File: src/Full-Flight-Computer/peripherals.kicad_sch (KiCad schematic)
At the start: 36 parts, among them P10 Micro_SD_Card, P8 USB, P9 1984659, Q5 QS5U17TR, Q6 QS5U17TR, U10 TS391IYLT, U11 TS391IYLT, U6 SST25VF040B-50-4I-S2AE-T, U7 RFM95W-868S2, U8 CP2102-GMR(QFN28), U9 TS391IYLT

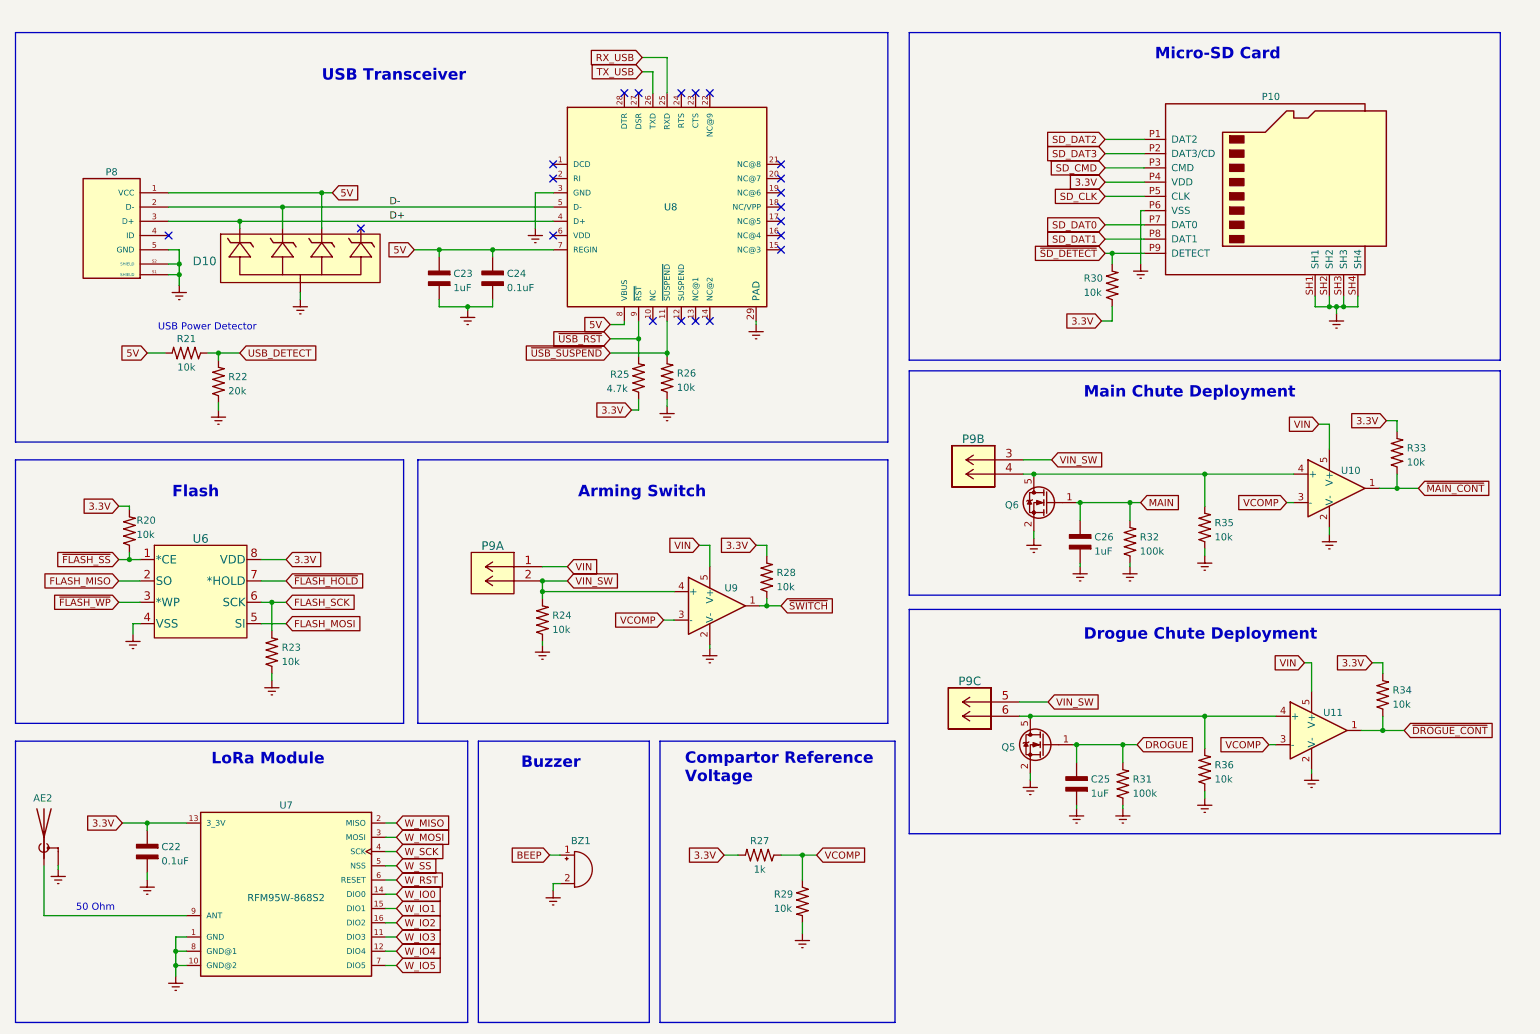
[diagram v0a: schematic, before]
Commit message: removed extra sections from schematic
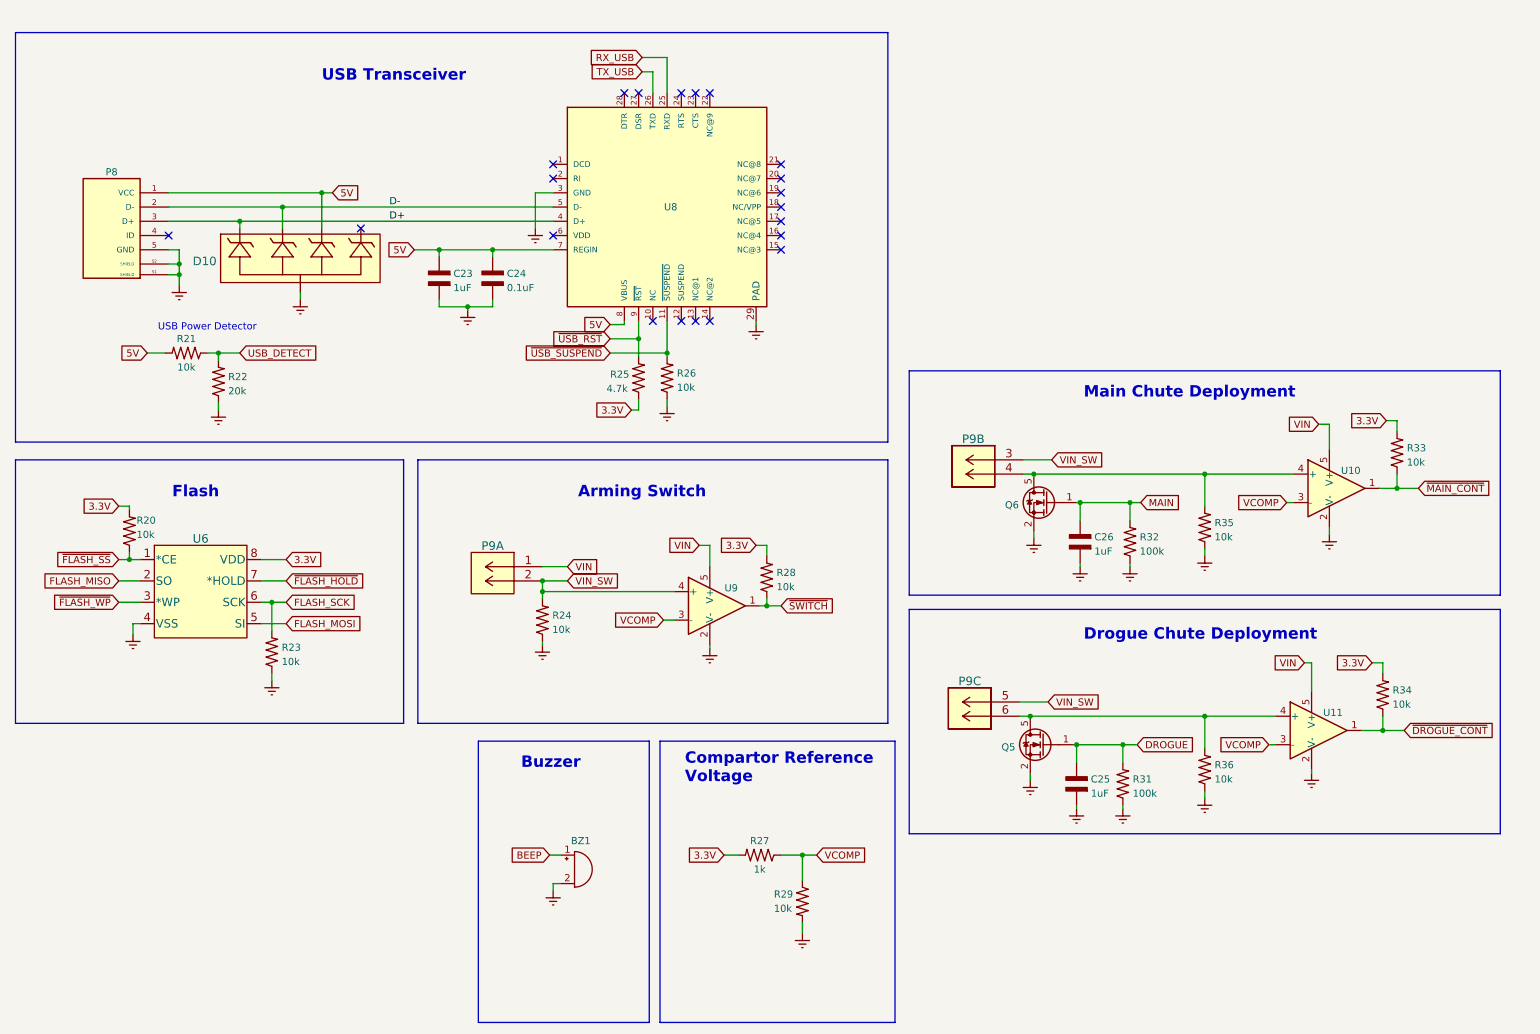
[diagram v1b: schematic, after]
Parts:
- removed AE2: 142-0701-851, Flight-Computer:142-0701-851, symbol Flight-Computer:142-0701-851
- removed C22: 0.1uF, Flight-Computer:CAP_0603, symbol Flight-Computer:CAP_0603
- removed P10: Micro_SD_Card, Flight-Computer:MEM2075-00-140-01-A, symbol Flight-Computer:Micro_SD_Card
- removed R30: 10k, Flight-Computer:RES_0603, symbol Flight-Computer:RES_0603
- removed U7: RFM95W-868S2, Flight-Computer:RFM95, symbol Flight-Computer:RFM95W-868S2
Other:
- note removed: "50 Ohm"
- note removed: "LoRa Module"
- note removed: "Micro-SD Card"

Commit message: fixed all schematic symbol links to link to correct lib file
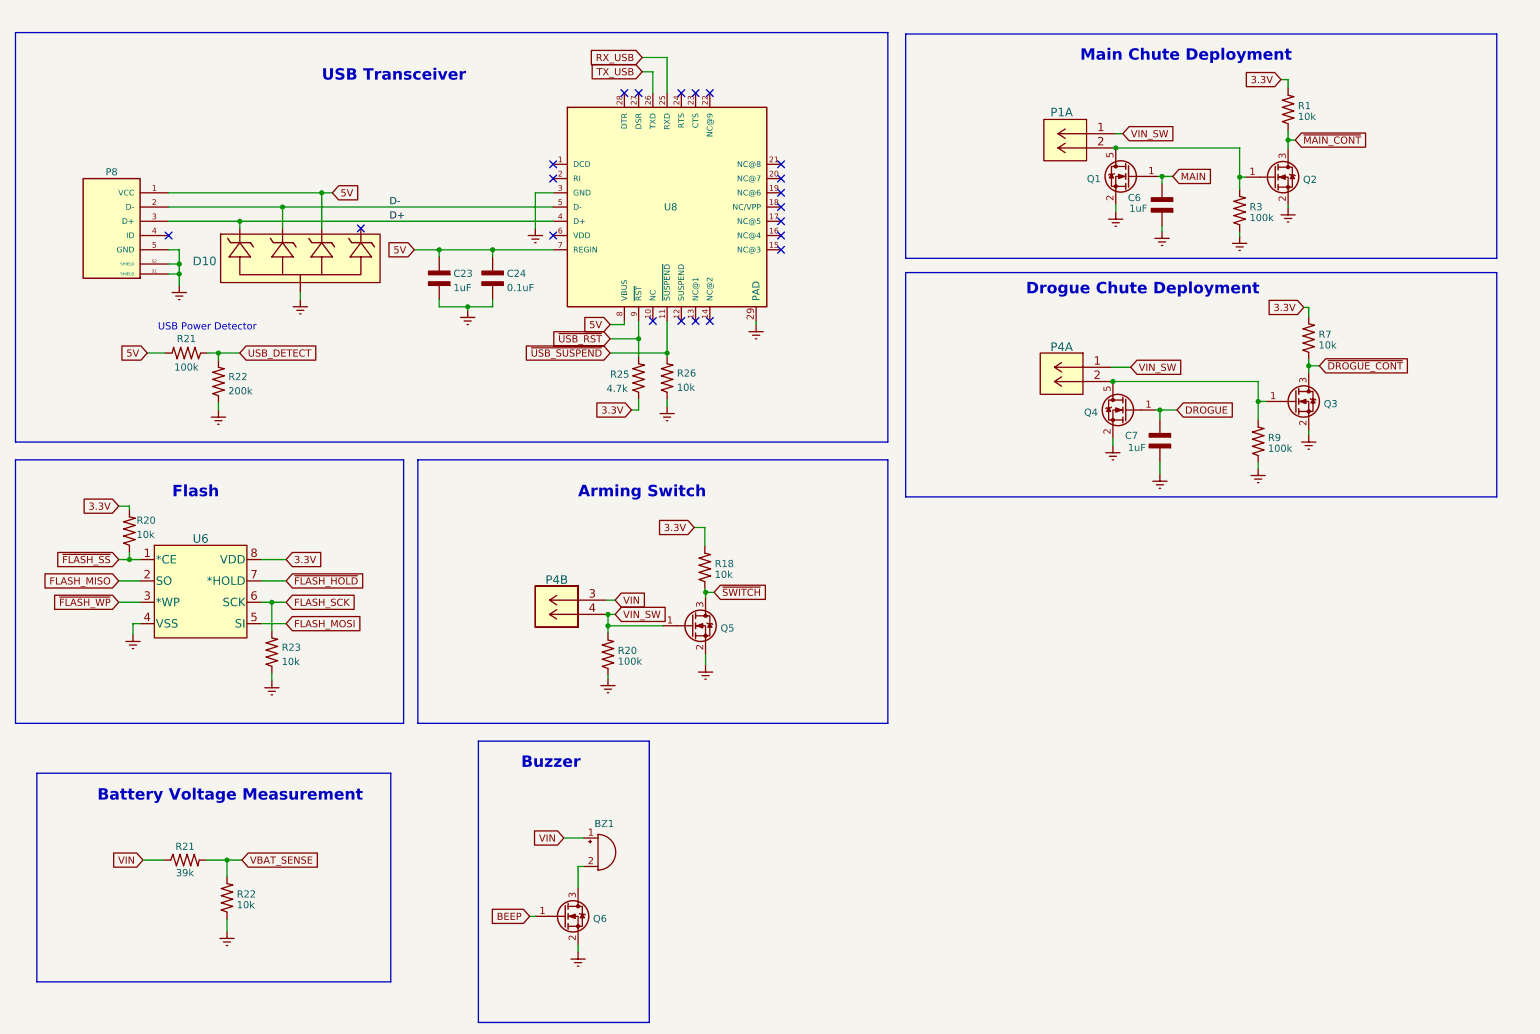
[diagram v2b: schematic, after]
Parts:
- removed C25, C26: 1uF, Flight-Computer:CAP_0603, symbol Flight-Computer:CAP_0603
- removed P9: 1984659, Flight-Computer:1984659, symbol Flight-Computer:1984659
- removed Q5, Q6: QS5U17TR, Flight-Computer:QS5U17TR, symbol Flight-Computer:QS5U17TR
- removed R24, R28, R29, R33, R34, R35, R36: 10k, Flight-Computer:RES_0603, symbol Flight-Computer:RES_0603
- removed R27: 1k, Flight-Computer:RES_0603, symbol Flight-Computer:RES_0603
- removed R31, R32: 100k, Flight-Computer:RES_0603, symbol Flight-Computer:RES_0603
- removed U10, U11, U9: TS391IYLT, Flight-Computer:TS391IYLT, symbol Flight-Computer:TS391IYLT
- added C6, C7: 1uF, Full-Flight-Computer:CAP_0402, symbol Full-Flight-Computer:CAP_0402
- added P1, P4: 1984659, Full-Flight-Computer:1546551-4, symbol Full-Flight-Computer:1546551-4
- added Q1, Q4: QS5U17TR, Full-Flight-Computer:QS5U17TR, symbol Full-Flight-Computer:QS5U17TR
- added Q2, Q3, Q5: 2N7002W-7-F, Full-Flight-Computer:2N7002W-7-F, symbol Full-Flight-Computer:2N7002W-7-F
- added Q6: 2N7002W-7-F, Base-Flight-Computer:2N7002W-7-F, symbol Flight-Computer-Lite:2N7002W-7-F
- added R1, R18, R22, R7: 10k, Full-Flight-Computer:RES_0402, symbol Full-Flight-Computer:RES_0402
- added R20, R3, R9: 100k, Full-Flight-Computer:RES_0402, symbol Full-Flight-Computer:RES_0402
- added R21: 39k, Full-Flight-Computer:RES_0402, symbol Full-Flight-Computer:RES_0402
- BZ1: footprint Flight-Computer:AT-1438-TWT-R -> Base-Flight-Computer:AT-1438-TWT-R
- C23, C24: footprint Flight-Computer:CAP_0603 -> Full-Flight-Computer:CAP_0402; symbol Flight-Computer:CAP_0603 -> Full-Flight-Computer:CAP_0402
- D10: footprint Flight-Computer:SP0504BAHTG -> Full-Flight-Computer:SP0504BAHTG; symbol Flight-Computer:SP0504BAHTG -> Full-Flight-Computer:SP0504BAHTG
- P8: footprint Flight-Computer:10118194-0001LF -> Full-Flight-Computer:10118194-0001LF; symbol Flight-Computer:USB -> Full-Flight-Computer:USB
- R20, R23, R25, R26: footprint Flight-Computer:RES_0603 -> Full-Flight-Computer:RES_0402; symbol Flight-Computer:RES_0603 -> Full-Flight-Computer:RES_0402
- R21: value 10k -> 100k; footprint Flight-Computer:RES_0603 -> Full-Flight-Computer:RES_0402; symbol Flight-Computer:RES_0603 -> Full-Flight-Computer:RES_0402
- R22: value 20k -> 200k; footprint Flight-Computer:RES_0603 -> Full-Flight-Computer:RES_0402; symbol Flight-Computer:RES_0603 -> Full-Flight-Computer:RES_0402
- U6: footprint Flight-Computer:SST25VF040B-50-4I-S2AE-T -> Full-Flight-Computer:SST25VF040B-50-4I-S2AE-T; symbol Flight-Computer:SST25VF040B-50-4I-S2AE-T -> Full-Flight-Computer:SST25VF040B-50-4I-S2AE-T
- U8: footprint Flight-Computer:CP2012-GMR -> Full-Flight-Computer:CP2012-GMR; symbol Flight-Computer:CP2102-GMR(QFN28) -> Full-Flight-Computer:CP2102-GMR
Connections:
- net 3.3V: now also R1.2, R18.2, R7.2
- net BEEP: now also Q6.1 (G); no longer BZ1.1 (-)
- net DROGUE: now also C7.1, Q4.1 (G)
- net Earth: now also C6.2, C7.2, Q1.2 (S), Q2.2 (S), Q3.2 (S), Q4.2 (S), Q5.2 (S), Q6.2 (S), R20.1, R22.1, R3.1, R9.1; no longer BZ1.2 (+)
- net MAIN: now also C6.1, Q1.1 (G)
- net VIN: now also BZ1.1 (-), P4.3 (5), R21.1
- net VIN_SW: now also P1.1 (5), P4.1 (5), P4.4 (6), Q5.1 (G), R20.2
- net ~{DROGUE_CONT}: now also Q3.3 (D), R7.1
- net ~{MAIN_CONT}: now also Q2.3 (D), R1.1
- net ~{SWITCH}: now also Q5.3 (D), R18.1
- new net: P4.2 (6), Q3.1 (G), Q4.5 (D), R9.2
- new net: BZ1.2 (+), Q6.3 (D)
- new net: P1.2 (6), Q1.5 (D), Q2.1 (G), R3.2
- new net VBAT_SENSE: R21.2, R22.2
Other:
- note added: "Battery Voltage Measurement"
- note removed: "Compartor Reference Voltage"

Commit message: added auxiliary ports for staging/redundant ejection charges
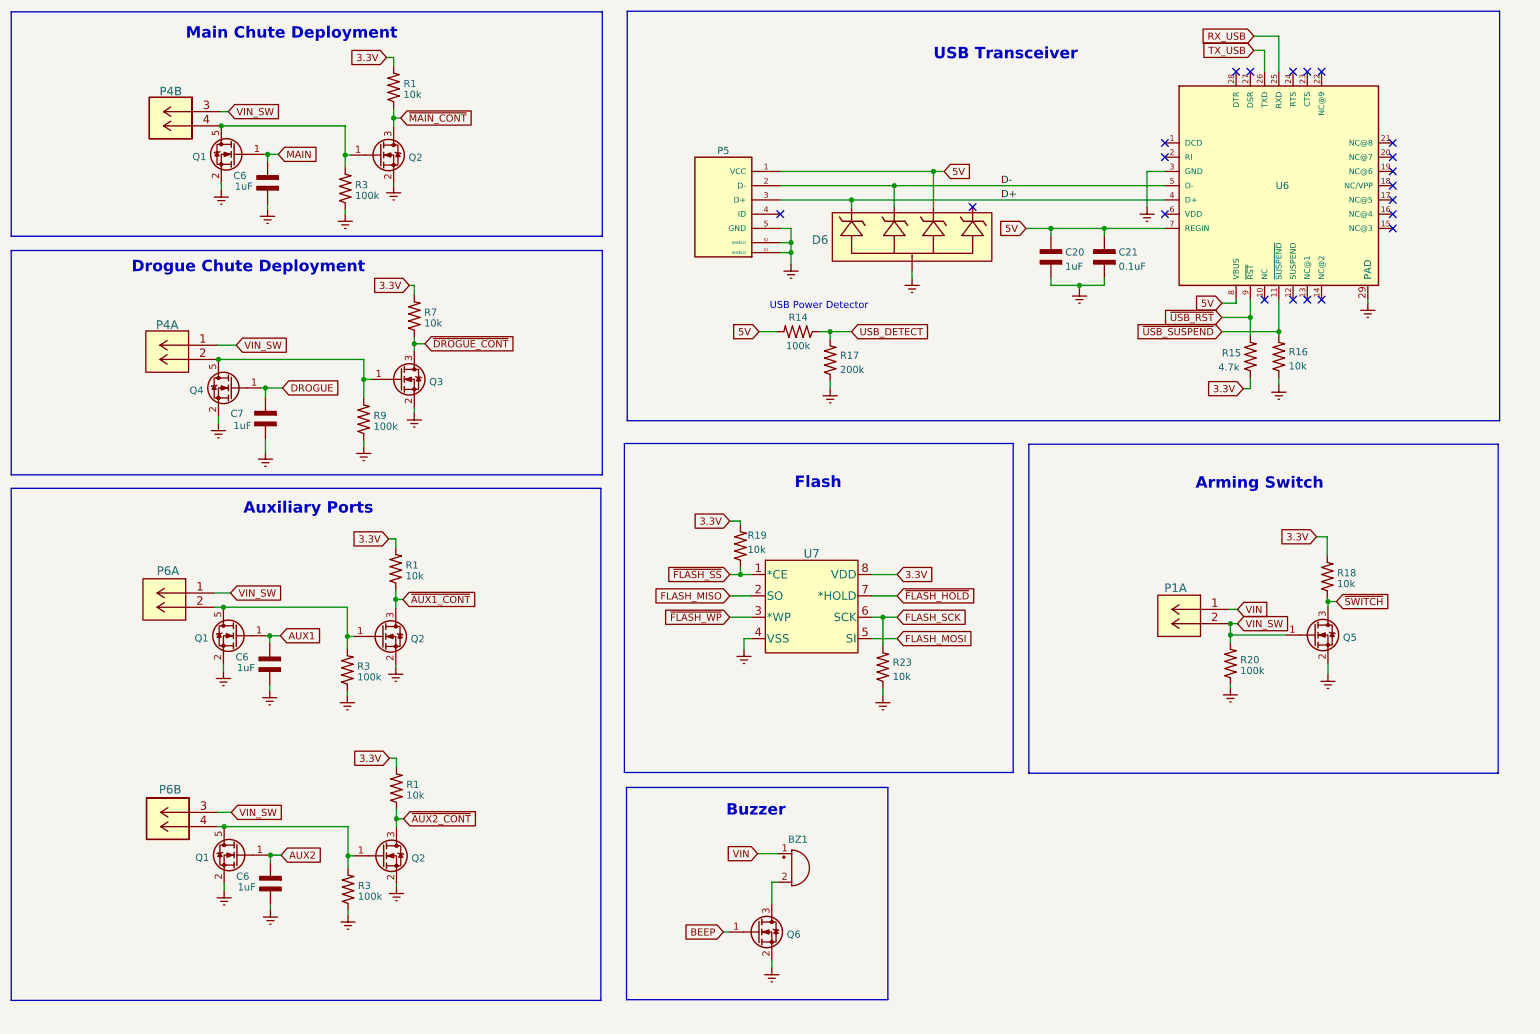
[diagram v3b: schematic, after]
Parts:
- removed R21: 39k, Full-Flight-Computer:RES_0402, symbol Full-Flight-Computer:RES_0402
- removed R22: 10k, Full-Flight-Computer:RES_0402, symbol Full-Flight-Computer:RES_0402
- added C6 (x2): 1uF, Full-Flight-Computer:CAP_0402, symbol Full-Flight-Computer:CAP_0402
- added P6: 1546551-4, Full-Flight-Computer:1546551-4, symbol Full-Flight-Computer:1546551-4
- added Q1 (x2): QS5U17TR, Full-Flight-Computer:QS5U17TR, symbol Full-Flight-Computer:QS5U17TR
- added Q2 (x2): 2N7002W-7-F, Full-Flight-Computer:2N7002W-7-F, symbol Full-Flight-Computer:2N7002W-7-F
- added R1 (x2): 10k, Full-Flight-Computer:RES_0402, symbol Full-Flight-Computer:RES_0402
- added R3 (x2): 100k, Full-Flight-Computer:RES_0402, symbol Full-Flight-Computer:RES_0402
- renumbered C23 to C20, C24 to C21, D10 to D6, P8 to P5, R21 to R14, R25 to R15, R26 to R16, R22 to R17, R20 to R19, U8 to U6, U6 to U7
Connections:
- net 3.3V: now also R1.2, R1.2
- net Earth: now also C6.2, C6.2, Q1.2 (S), Q1.2 (S), Q2.2 (S), Q2.2 (S), R3.1, R3.1
- net VIN: now also P1.1 (5); no longer P4.3 (5)
- net VIN_SW: now also P1.2 (6), P4.3 (5), P6.1 (5), P6.3 (5); no longer P1.1 (5), P4.4 (6)
- net at Q1.5 (D), Q2.1 (G), R3.2: now also P4.4 (6); no longer P1.2 (6)
- new net: P6.4 (6), Q1.5 (D), Q2.1 (G), R3.2
- new net: P6.2 (6), Q1.5 (D), Q2.1 (G), R3.2
- new net AUX1: C6.1, Q1.1 (G)
- new net AUX2: C6.1, Q1.1 (G)
- new net ~{AUX1_CONT}: Q2.3 (D), R1.1
- new net ~{AUX2_CONT}: Q2.3 (D), R1.1
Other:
- note added: "Auxiliary Ports"
- note removed: "Battery Voltage Measurement"
- moved on the sheet: BZ1, C20, C21, C6, C7, D6, P1A, P4A, P4B, P5, Q1, Q2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

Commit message: redid component designators and updated BOM
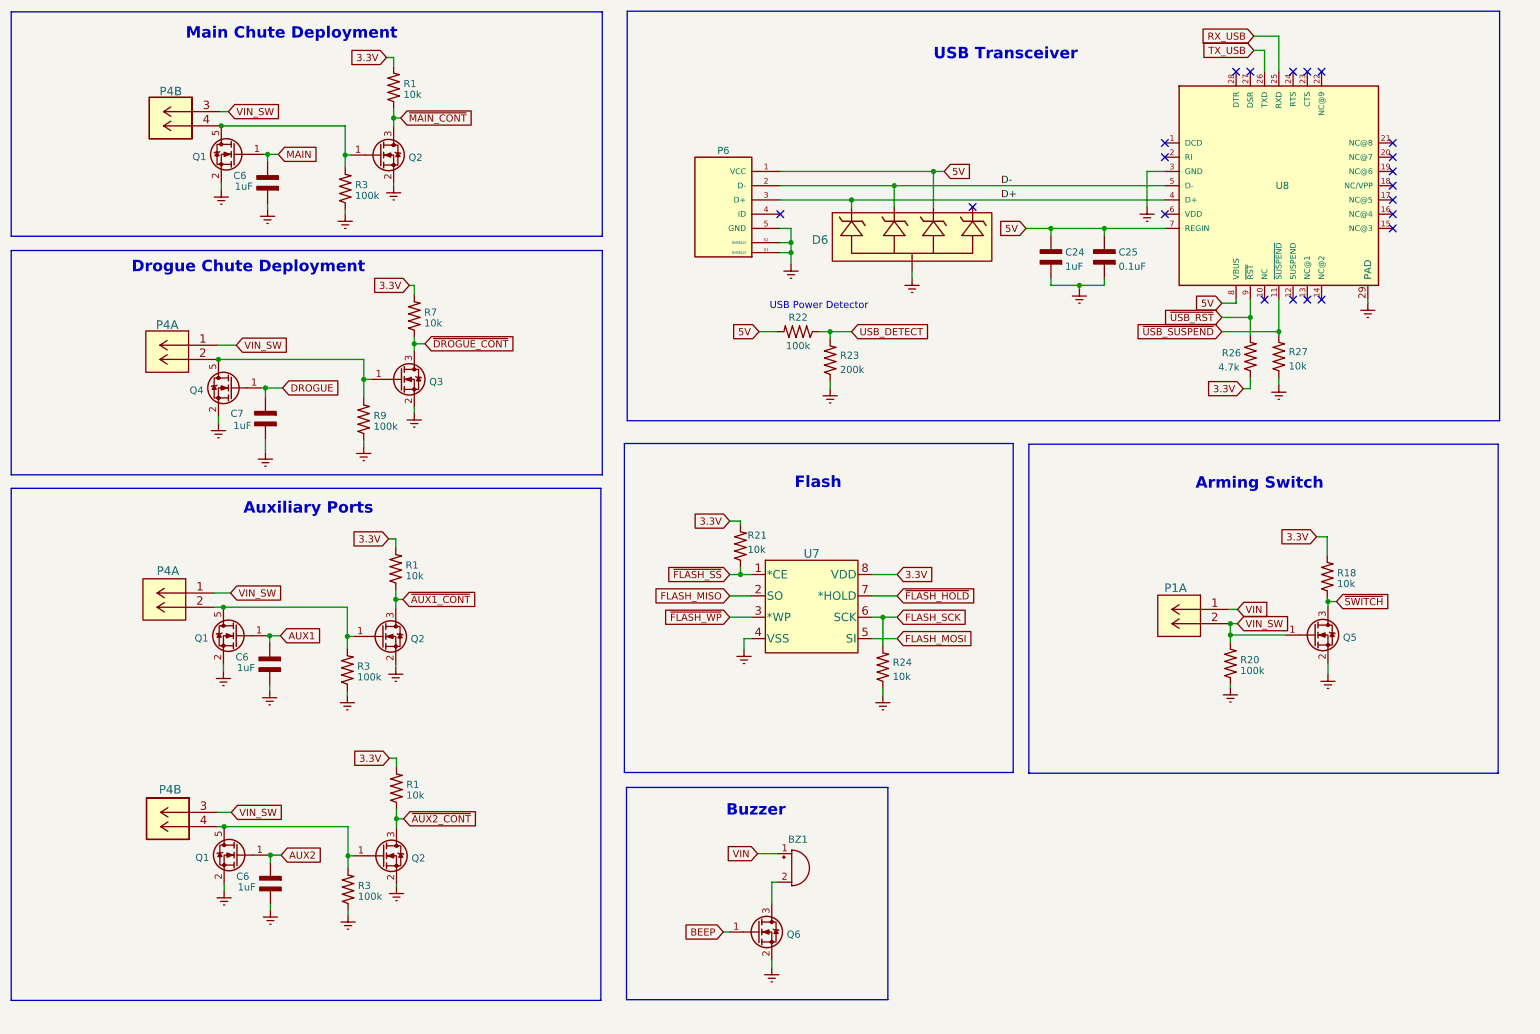
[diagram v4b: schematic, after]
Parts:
- BZ1: footprint Base-Flight-Computer:AT-1438-TWT-R -> Full-Flight-Computer:AT-1438-TWT-R; symbol Flight-Computer:AT-1438-TWT-R -> Full-Flight-Computer:AT-1438-TWT-R
- Q6: footprint Base-Flight-Computer:2N7002W-7-F -> Full-Flight-Computer:2N7002W-7-F; symbol Flight-Computer-Lite:2N7002W-7-F -> Full-Flight-Computer:2N7002W-7-F
- renumbered C20 to C24, C21 to C25, P6 to P4, P5 to P6, R19 to R21, R14 to R22, R17 to R23, R23 to R24, R15 to R26, R16 to R27, U6 to U8

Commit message: completed initial layout
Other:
- moved on the sheet: C6, P4A, Q1, Q2, R1, R3
